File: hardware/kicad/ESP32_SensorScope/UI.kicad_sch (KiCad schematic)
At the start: 4 parts, among them U16 74LVC1G240DBVRG4

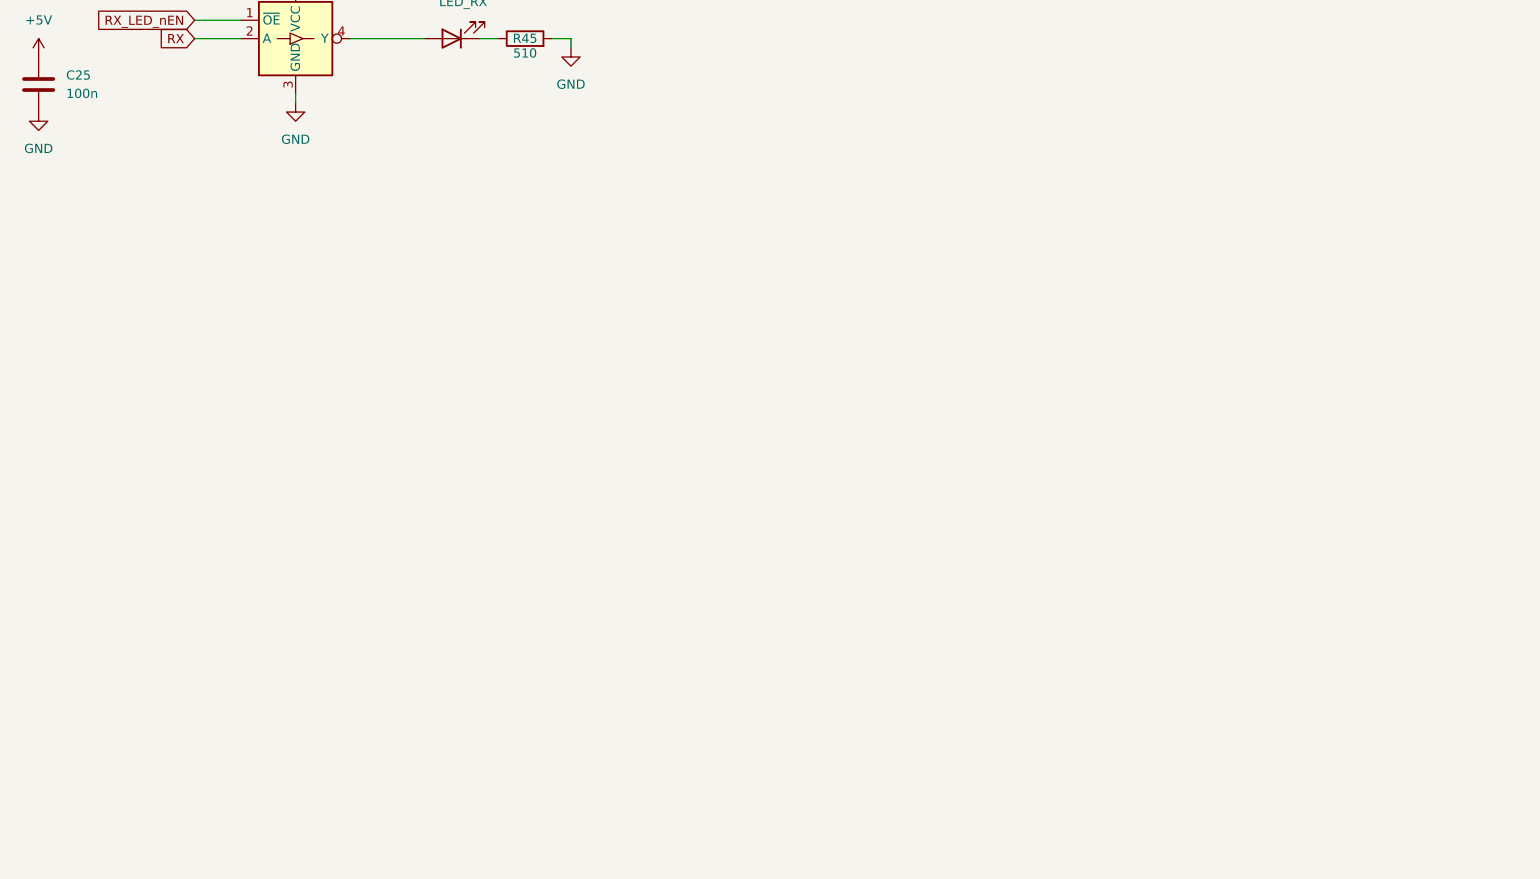
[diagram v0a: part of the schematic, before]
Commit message: Adde LCD Part
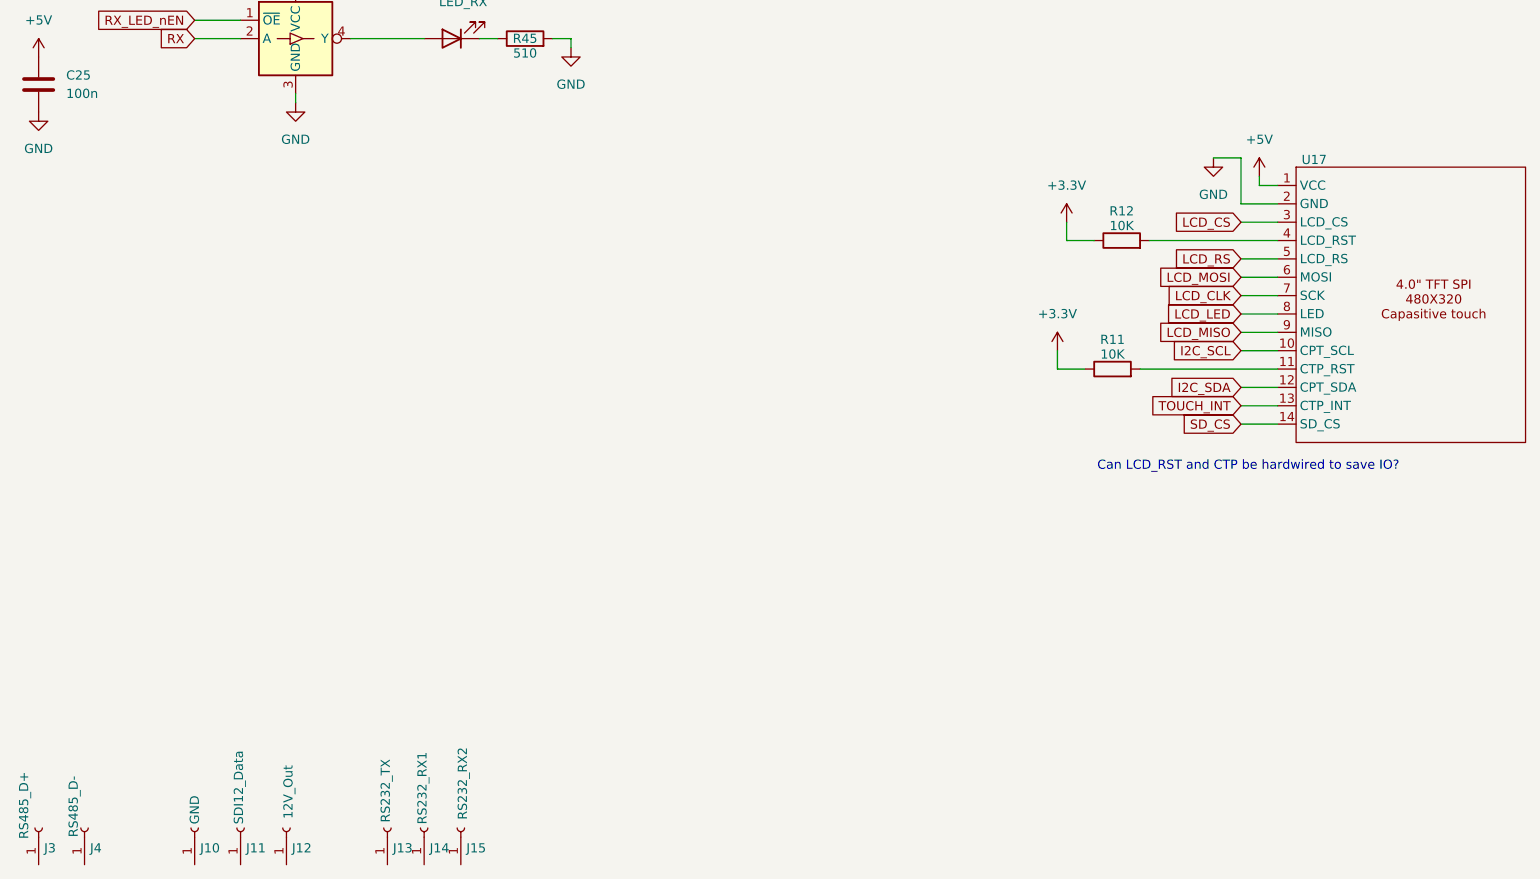
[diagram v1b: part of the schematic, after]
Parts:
- added J10: GND, symbol Connector:Conn_01x01_Socket
- added J11: SDI12_Data, symbol Connector:Conn_01x01_Socket
- added J12: 12V_Out, symbol Connector:Conn_01x01_Socket
- added J13: RS232_TX, symbol Connector:Conn_01x01_Socket
- added J14: RS232_RX1, symbol Connector:Conn_01x01_Socket
- added J15: RS232_RX2, symbol Connector:Conn_01x01_Socket
- added J3: RS485_D+, symbol Connector:Conn_01x01_Socket
- added J4: RS485_D-, symbol Connector:Conn_01x01_Socket
- added R11, R12: 10K, symbol Device:R
- added U17: ~, My_library:MSP4031, symbol My_library:MSP4031
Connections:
- net +5V: now also U17.1 (VCC)
- net GND: now also U17.2 (GND)
- new net: R12.2, U17.4 (LCD_RST)
- new net: R11.2, U17.11 (CTP_RST)
- new net +3.3V: R11.1, R12.1
- new net I2C_SCL: U17.10 (CPT_SCL)
- new net I2C_SDA: U17.12 (CPT_SDA)
- new net LCD_CLK: U17.7 (SCK)
- new net LCD_CS: U17.3 (LCD_CS)
- new net LCD_LED: U17.8 (LED)
- new net LCD_MISO: U17.9 (MISO)
- new net LCD_MOSI: U17.6 (MOSI)
- new net LCD_RS: U17.5 (LCD_RS)
- new net SD_CS: U17.14 (SD_CS)
- new net TOUCH_INT: U17.13 (CTP_INT)
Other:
- note added: "Can LCD_RST and CTP be hardwired to save IO?"

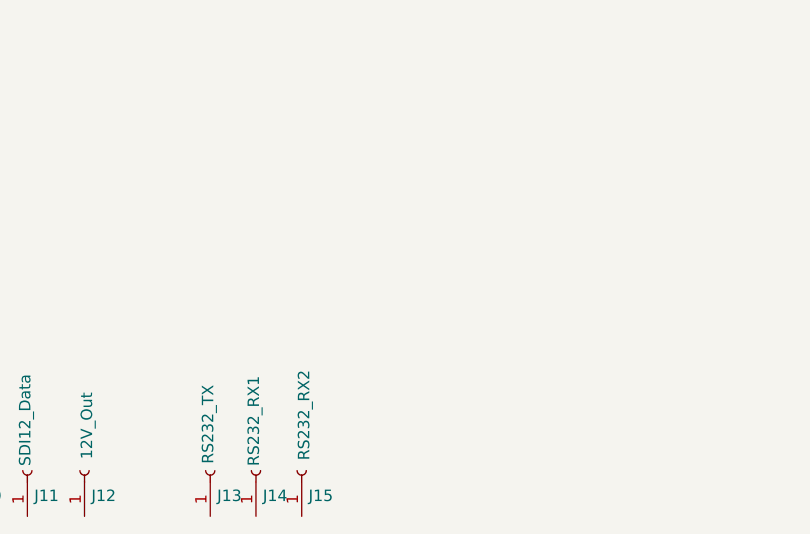
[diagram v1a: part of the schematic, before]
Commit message: updated 4-20mA interface
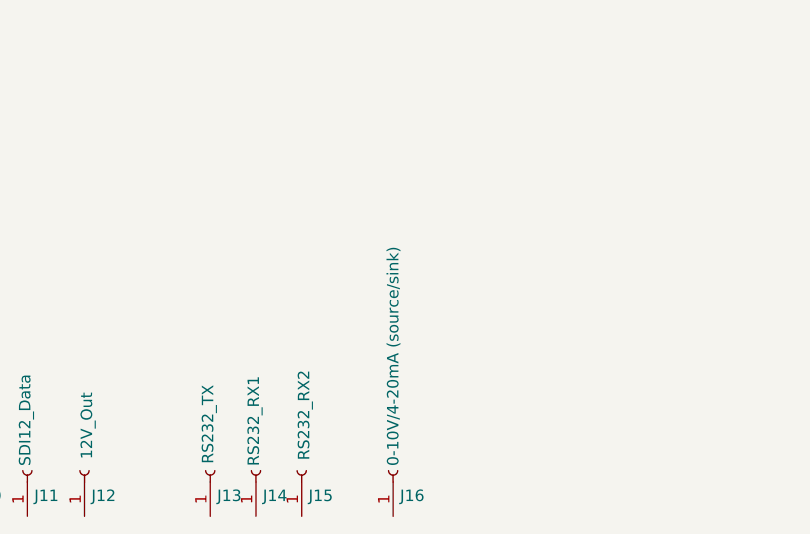
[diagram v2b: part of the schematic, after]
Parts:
- added J16: 0-10V/4-20mA (source/sink), symbol Connector:Conn_01x01_Socket
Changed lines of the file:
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@@
+	)
+	(symbol
+		(lib_id "Connector:Conn_01x01_Socket")
+		(at 101.6 142.24 90)
+		(unit 1)
+		(exclude_from_sim no)
+		(in_bom yes)
+		(on_board yes)
+		(dnp no)
+		(property "Reference" "J16"
+			(at 102.362 145.034 90)
+			(effects
+				(font
+					(size 1.27 1.27)
+				)
+				(justify right)
+			)
+		)
+		(property "Value" "0-10V/4-20mA (source/sink)"
+			(at 101.6 141.732 0)
+			(effects
+				(font
+					(size 1.27 1.27)
+				)
+				(justify left)
+			)
+		)
+		(property "Footprint" ""
+			(at 101.6 142.24 0)
+			(effects
+				(font
+					(size 1.27 1.27)
+				)
+				(hide yes)
+			)
+		)
+		(property "Datasheet" "~"
+			(at 101.6 142.24 0)
+			(effects
+				(font
+					(size 1.27 1.27)
+				)
+				(hide yes)
+			)
+		)
+		(property "Description" "Generic connector, single row, 01x01, script generated"
+			(at 101.6 142.24 0)
+			(effects
+				(font
+					(size 1.27 1.27)
+				)
+				(hide yes)
+			)
+		)
+		(pin "1"
+		)
+		(instances
+			(project "ESP32_SensorScope"
+				(path "/53b18f60-802b-4114-ad1b-2672cfed64a1/7bfcde62-1fc6-4742-9ded-14bc7dc34229"
+					(reference "J16")
+					(unit 1)
+				)
+			)
+		)
 	)
 	(symbol

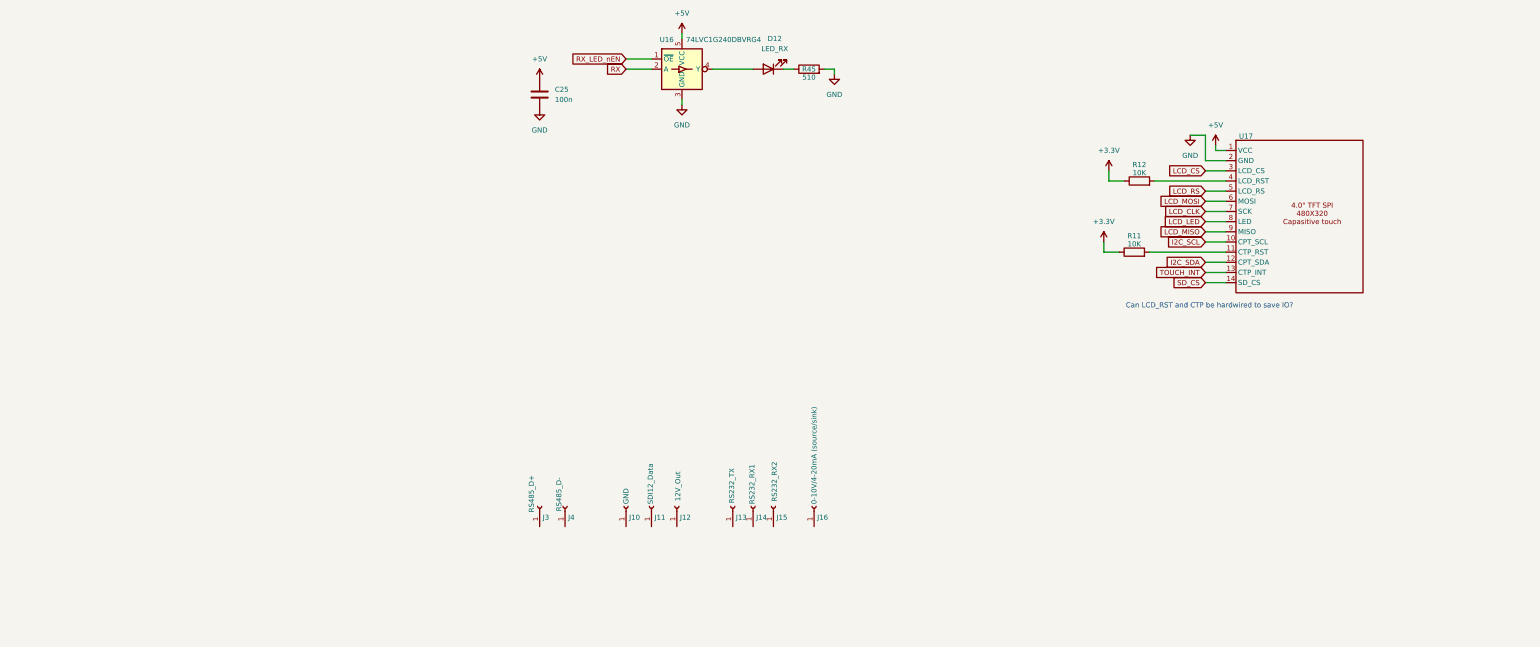
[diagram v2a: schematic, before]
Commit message: som updates on the schematics
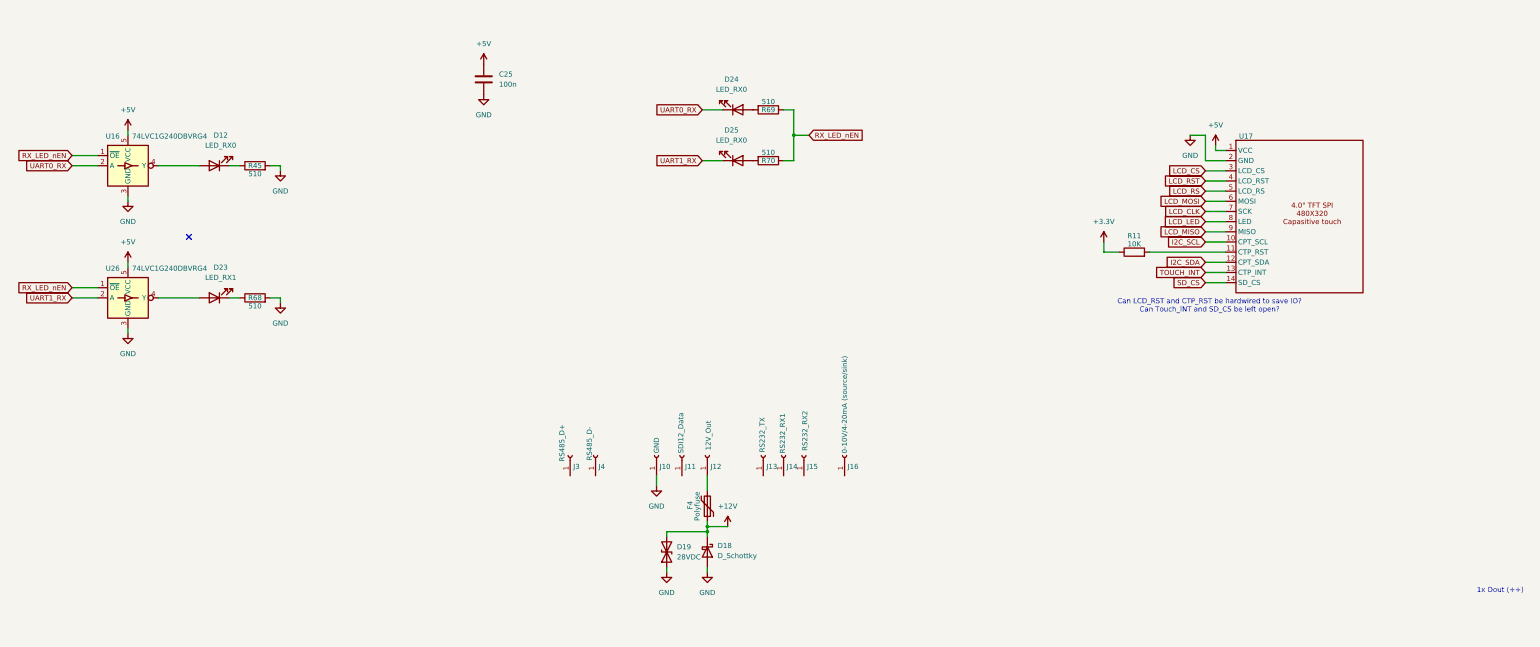
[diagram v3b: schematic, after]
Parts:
- removed R12: 10K, symbol Device:R
- added D18: D_Schottky, symbol Device:D_Schottky
- added D19: 28VDC, symbol Device:D_TVS
- added D23: LED_RX1, symbol Device:LED
- added D24, D25: LED_RX0, symbol Device:LED
- added F4: Polyfuse, symbol Device:Polyfuse
- added R68, R69, R70: 510, symbol Device:R
- added U26: 74LVC1G240DBVRG4, Package_TO_SOT_SMD:SOT-23-5, symbol SN74LVC1G240:74LVC1G240DBVRG4
- D12: value LED_RX -> LED_RX0
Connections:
- net +5V: now also U26.5 (VCC)
- net GND: now also J10.1 (Pin_1), D18.2 (A), D19.1 (A1), R68.2, U26.3 (GND)
- net RX_LED_nEN: now also R69.1, R70.1, U26.1 (~{OE})
- net LCD_RST: now reaches U17.4 (LCD_RST)
- net at J12.1 (Pin_1): now also F4.2
- net RX renamed UART0_RX
- net UART0_RX: now also D24.1 (K)
- new net: D24.2 (A), R69.2
- new net: D23.2 (A), U26.4 (Y)
- new net: D23.1 (K), R68.1
- new net: D25.2 (A), R70.2
- new net +12V: D18.1 (K), D19.2 (A2), F4.1
- new net UART1_RX: D25.1 (K), U26.2 (A)
- no-connect marks 0 -> 1
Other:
- note added: "1x Dout (++)"
- note added: "Can LCD_RST and CTP_RST be hardwired to save IO? Can Touch_INT and SD_CS be left open?"
- note removed: "Can LCD_RST and CTP be hardwired to save IO?"
- moved on the sheet: C25, D12, J10, J11, J12, J13, J14, J15, J16, J3, J4, R45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

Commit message: updatet schematic
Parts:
- removed C25: 100n, symbol Device:C
- removed D12: LED_RX0, symbol Device:LED
- removed D23: LED_RX1, symbol Device:LED
- removed R45, R68: 510, symbol Device:R
- removed U16, U26: 74LVC1G240DBVRG4, Package_TO_SOT_SMD:SOT-23-5, symbol SN74LVC1G240:74LVC1G240DBVRG4
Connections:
- net RS232_RX2: now reaches J15.1 (Pin_1)
- net RS232_TX: now reaches J13.1 (Pin_1)
- net RS485_D+: now reaches J3.1 (Pin_1)
- net SDI12: now reaches J11.1 (Pin_1)
- net 4-20mA OUTPUT (Sourse/sink): now reaches J16.1 (Pin_1)
- net RS485_D-: now reaches J4.1 (Pin_1)
- net RS232_RX1: now reaches J14.1 (Pin_1)
- no-connect marks 1 -> 0
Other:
- note added: "I2C address: 111 0000"
- moved on the sheet: D18, D19, F4, R11

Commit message: addet some footprints"
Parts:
- D18: footprint (none) -> Diode_SMD:D_SMA
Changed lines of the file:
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@@
 			)
 		)
-		(property "Footprint" ""
+		(property "Footprint" "Diode_SMD:D_SMA"
 			(at 74.93 163.83 0)
 			(effects
